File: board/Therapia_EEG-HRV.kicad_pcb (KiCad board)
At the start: 4 copper layers, 61.8 x 45 mm, 141 parts, among them J1 USB-C_16P, J2 Header_2x6

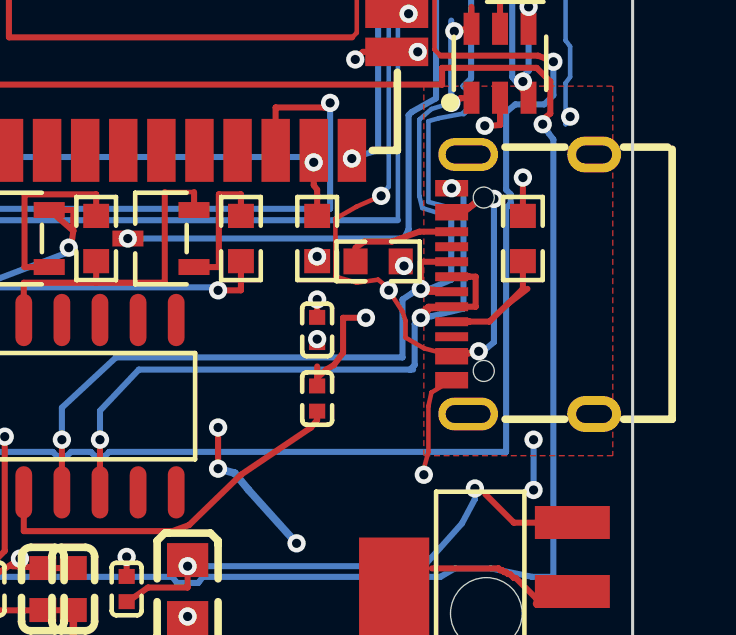
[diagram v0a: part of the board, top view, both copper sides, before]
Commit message: S5 L4: clear the USB-C peg holes PEG1 and PEG2
PEG1 was a clearance problem and is fixed as one: the VBUS via retreated and
four tracks re-routed, all clear by 0.22 mm or better against a 0.2 mm rule.

PEG2 was a topology problem. VBUS reached J1 pin 11 only by squeezing east
between the peg and the ESP32 UART pair, and every piece of that squeeze sat
inside the peg's ring -- both endpoints of each track were in there, so
re-routing between them could not help, and the via had no legal site within
2.5 mm. Its drill overlapped the peg's by 0.16 mm, so the barrel could not
form and VBUS would not have reached the board at all. Those seven pieces are
deleted and pin 11 now feeds from the west, 2.03 mm to the VBUS via that was
already there.

J1 pins 1 and 12 are the connector's own ground pads, 0.1712 mm from the
connector's own peg holes -- vendor footprint geometry, 0.0288 mm short of the
rule. Trimmed 0.05 mm a side along the axis facing the peg: 1.10 -> 1.00 mm of
land length, gap now 0.2211 mm. Nothing else about the footprint changed.

DRC errors 56 -> 30; hole_to_hole 4 -> 0, hole_clearance 25 -> 1. unconnected 0.

Co-Authored-By: Claude Fable 5 <noreply@anthropic.com>
Claude-Session: https://claude.ai/code/session_01431Pn2abKuPv9KnYCZmkiJ
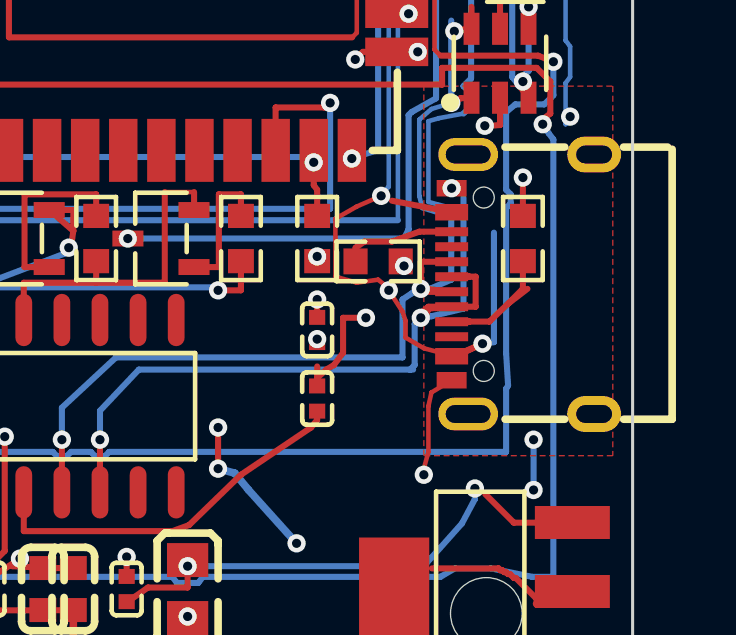
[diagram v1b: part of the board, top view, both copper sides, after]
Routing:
- net USB_VBUS_RAW: track 59.0 -> 58.1 mm, vias 5 -> 4

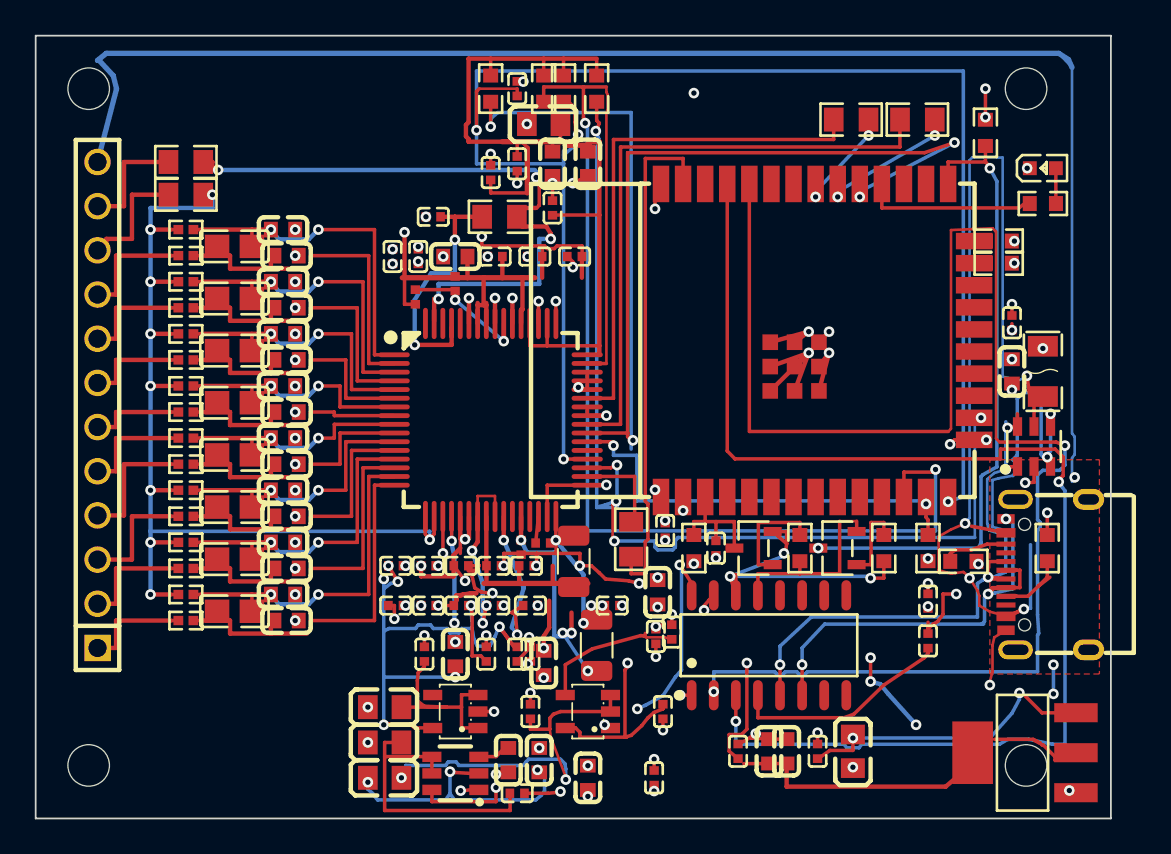
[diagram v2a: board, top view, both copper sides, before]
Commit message: S5 L5: pull apart the remaining clearance pinches
Found geometrically rather than from the DRC report -- lib/repair.clearance_pairs
asks the same SHAPE::Collide question DRC does and hands back the real items and
the real gap, instead of an item's anchor at the other end of an 11 mm track.

27 of 28 pinches fixed: 14 via retreats, 9 track detours, and 4 footprint nudges
of 0.05-0.15 mm (C_AVSS_B, C_3V3_H, C_VREFP_10n, C_RST_DLY) where both sides
were pads and nothing else could move. DRC errors 28 -> 4, unconnected 0,
contract parity unchanged.

The one left is a pinch the C_RST_DLY nudge created between that part's ground
pad and the ADS_RESET_N track; the loop marks a pair done once it has acted on
it, so a violation re-created later needs another pass. S6 is that pass.

Co-Authored-By: Claude Fable 5 <noreply@anthropic.com>
Claude-Session: https://claude.ai/code/session_01431Pn2abKuPv9KnYCZmkiJ
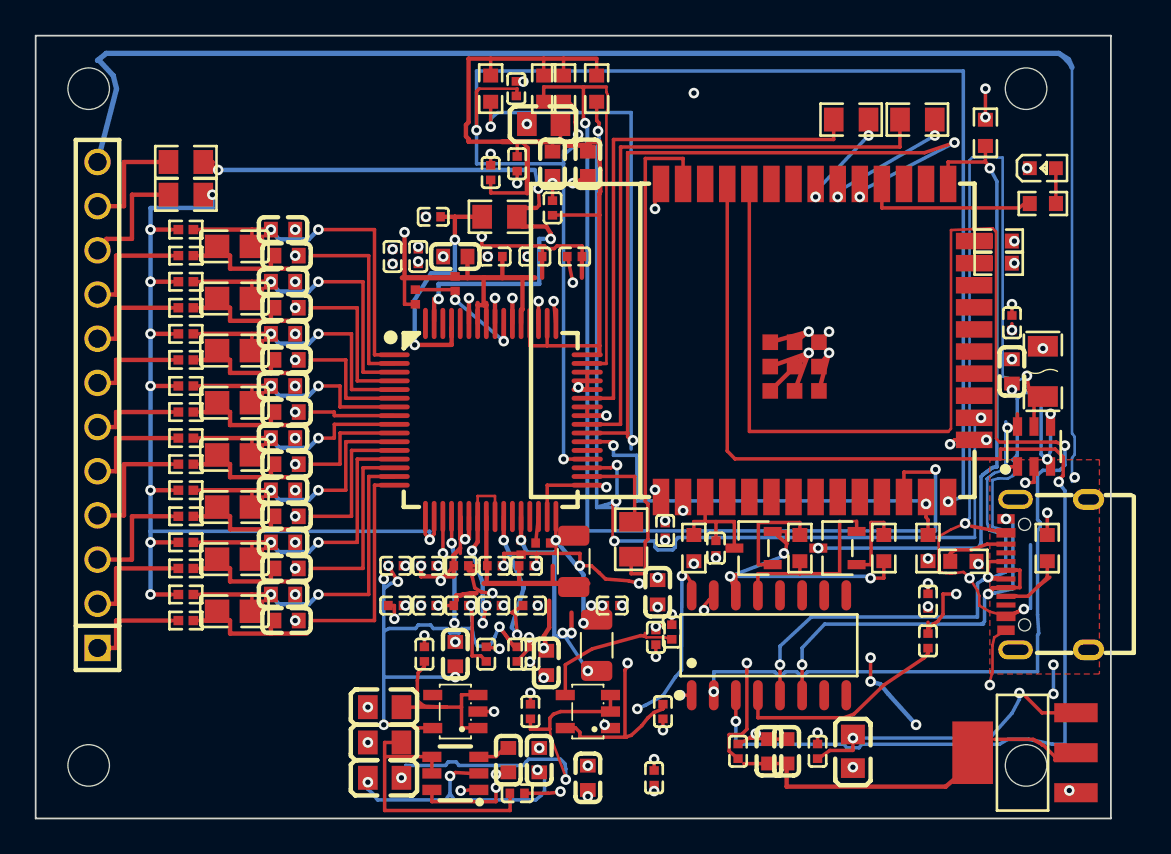
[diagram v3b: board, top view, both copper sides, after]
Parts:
- moved C_AVSS_B 0.15 mm to (149.4, 116.1)
- moved C_RST_DLY 0.05 mm to (147.6, 83.0)
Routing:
- net ADS_DRDY_N: track 73.2 -> 96.4 mm
- net AVDD: track 52.0 -> 54.1 mm
- net ESP_IO0: track 35.6 -> 36.6 mm
- net USB_5V: track 15.6 -> 14.6 mm
- net USB_DP: track 33.4 -> 34.0 mm
